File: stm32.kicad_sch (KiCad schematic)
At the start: 92 parts, among them J1 USB_B_Mini, J4 Conn_ST_STDC14, J5 Conn_02x20_Odd_Even, J7 TC2030 - TAG Connect, Q5 SI2301CDS-T1-GE3, SW1 SW_Push, SW2 SW_Push, U3 STM32F427V_G-I_Tx, X1 8MHz 20pF

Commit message: pre quilter - actually saved
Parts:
- U3: symbol MCU_ST_STM32F4:STM32F427V_G-I_Tx -> dnt:STM32F427V_G-I_Tx-mod
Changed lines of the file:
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@@
 			)
 		)
-		(property "Description" "20V 3.1A 112mΩ@4.5V,2.8A 1V@250uA 1PCSPChannel SOT-23 MOSFETs ROHS"
+		(property "Description" "Generic N-Channel Power MOSFET"
 			(at 349.25 193.04 0)
 			(effects
@@
 	)
 	(symbol
-		(lib_id "MCU_ST_STM32F4:STM32F427V_G-I_Tx")
+		(lib_id "dnt:STM32F427V_G-I_Tx-mod")
 		(at 163.83 158.75 0)
 		(unit 1)

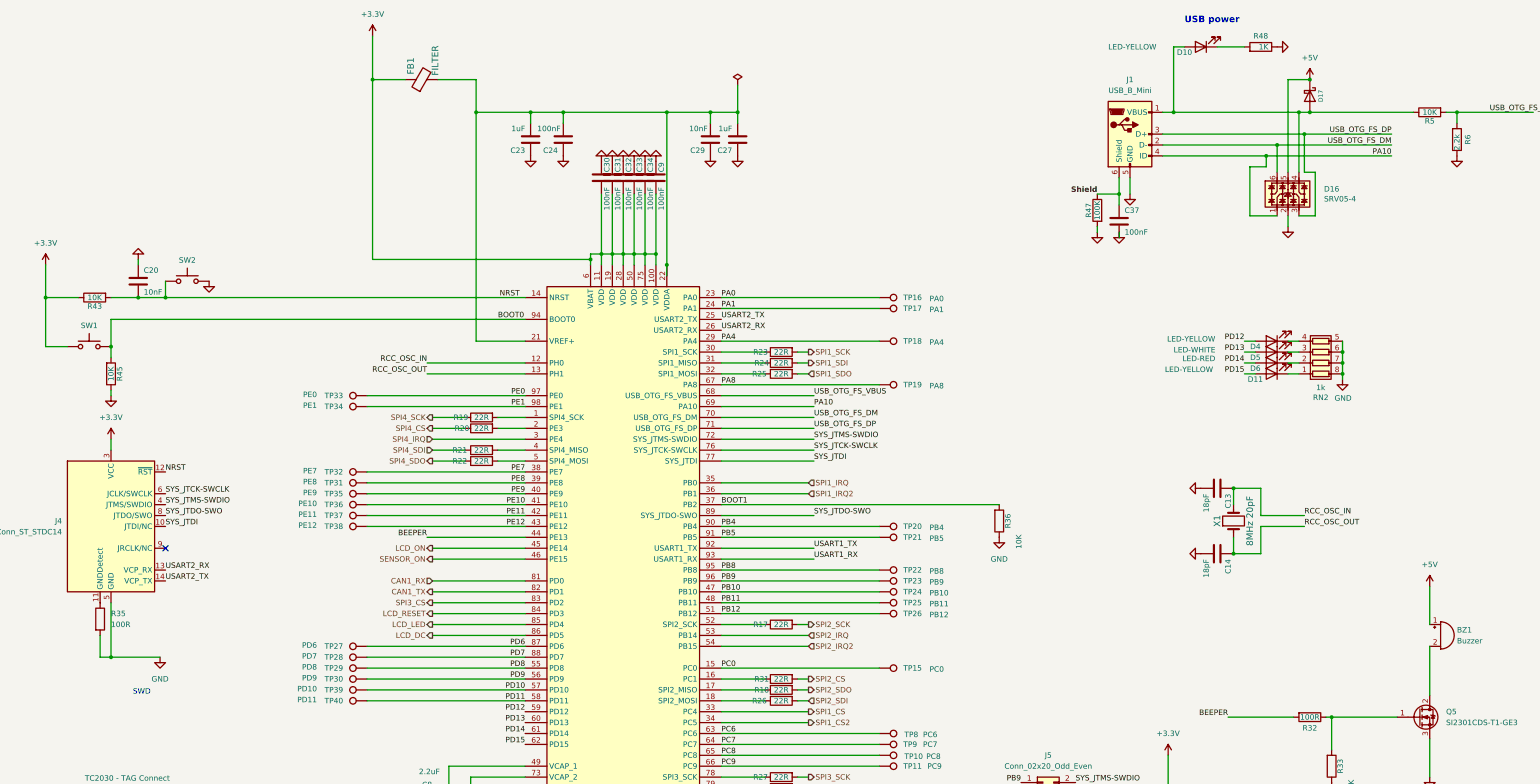
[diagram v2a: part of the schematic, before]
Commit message: smaller caps remove ringing resistors
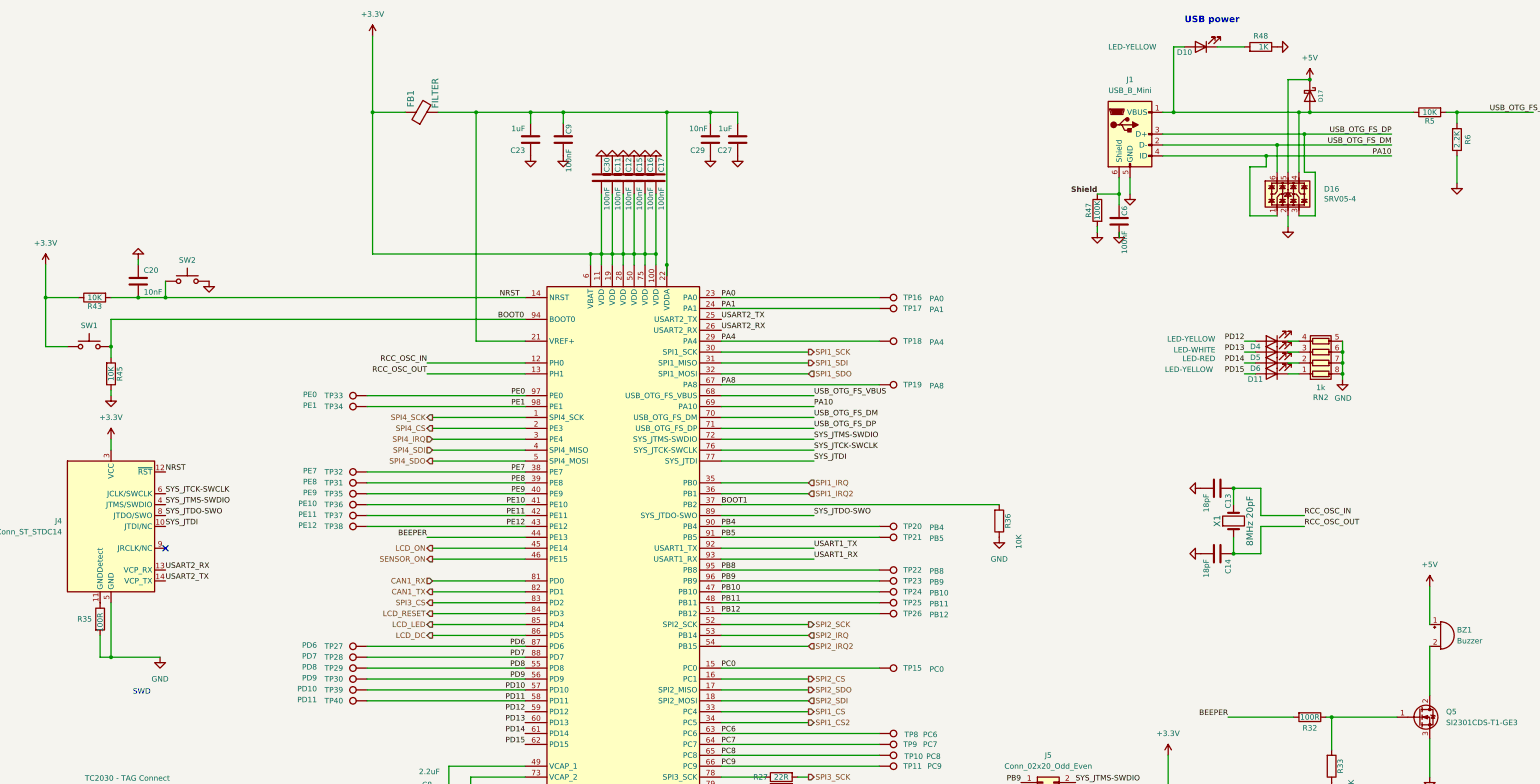
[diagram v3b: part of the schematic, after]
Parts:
- removed C24, C31, C32, C33, C34, C37: 100nF, Capacitor_SMD:C_0603_1608Metric, symbol Device:C
- removed R17, R18, R19, R20, R21, R22, R23, R24, R25, R26, R31: 22R, Resistor_SMD:R_0603_1608Metric, symbol Device:R
- added C11, C12, C15, C16, C17, C6: 100nF, Capacitor_SMD:C_01005_0402Metric, symbol Device:C
- C1: Manufacturer MURATA -> (none); PageName stm32f407_board -> (none); Part # GRM188R6YA225KA12D -> (none); VEND DIGI -> (none); VEND# 490-7204-1-ND -> (none)
- C13: PageName stm32f407_board -> (none); VEND DIGI -> (none); VEND# 1276-1089-1-ND -> (none)
- C14: PageName stm32f407_board -> (none); VEND DIGI -> (none); VEND# 1276-1089-1-ND -> (none); Voltage (none) -> 50V
- C20, C29: Manufacturer KEMET -> (none); Part # C0603C103K1RACTU -> (none); VEND DIGI -> (none); VEND# 399-3189-1-ND -> (none); Voltage (none) -> 50V
- C30, C9: footprint Capacitor_SMD:C_0603_1608Metric -> Capacitor_SMD:C_01005_0402Metric; LCSC C14663 -> C1525; Manufacturer KEMET -> Samsung; PageName stm32f407_board -> (none); Part # C0603C104J5RACTU -> (none); VEND DIGI -> (none); VEND# 399-7844-1-ND -> (none); Voltage (none) -> 16V
- R32: LCSC C21190 -> C22775; Manufacturer StackPole -> (none); Part # RMCF0603JJ1K00 -> (none); VEND DIGI -> (none); VEND# RMCF0603JJ1K00CT-ND -> (none)
- R33, R36, R43, R45, R5: Manufacturer StackPole -> (none); Part # RMCF0603JT10K0 -> (none); VEND DIGI -> (none); VEND# RMCF0603JT10K0CT-ND -> (none)
- R35: LCSC (none) -> C22775
- R47: Manufacturer StackPole -> (none); PageName stm32f407_board -> (none); Part # RMCF0603JT100K -> (none); VEND DIGI -> (none); VEND# RMCF0603JT100KCT-ND -> (none)
- R48: LCSC C4190 -> C21190
- R6: value 2.2k -> 2.2K; Manufacturer StackPole -> (none); PageName stm32f407_board -> (none); Part # RMCF0603FT2K20 -> (none); VEND DIGI -> (none); VEND# RMCF0603FT2K20CT-ND -> (none)
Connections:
- net +3.3V: now also C11.2, C12.2, C15.2, C16.2, C17.2; no longer C9.2
- net GND: now also C9.2, C11.1, C12.1, C15.1, C16.1, C17.1, C6.2; no longer C9.1
- net SPI1_SCK: now also U3.30 (PA5)
- net SPI1_SDI: now also U3.31 (PA6)
- net SPI1_SDO: now also U3.32 (PA7)
- net SPI2_CS: now also U3.16 (PC1)
- net SPI2_SCK: now also U3.52 (PB13)
- net SPI2_SDI: now also U3.18 (PC3)
- net SPI2_SDO: now also U3.17 (PC2)
- net SPI4_CS: now also U3.2 (PE3)
- net SPI4_SCK: now also U3.1 (PE2)
- net SPI4_SDI: now also U3.4 (PE5)
- net SPI4_SDO: now also U3.5 (PE6)
- net Shield: now also C6.1
- net at C23.2, C27.2, C29.2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: now also C9.1
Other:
- moved on the sheet: FB1

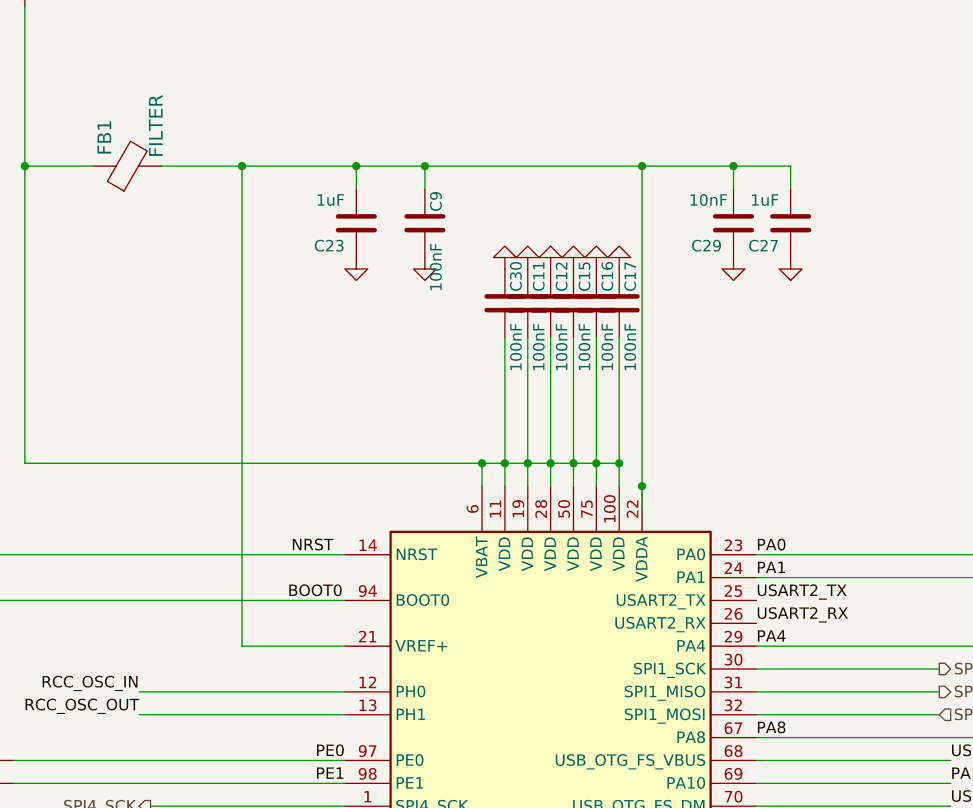
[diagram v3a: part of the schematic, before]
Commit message: add tp  move leds +
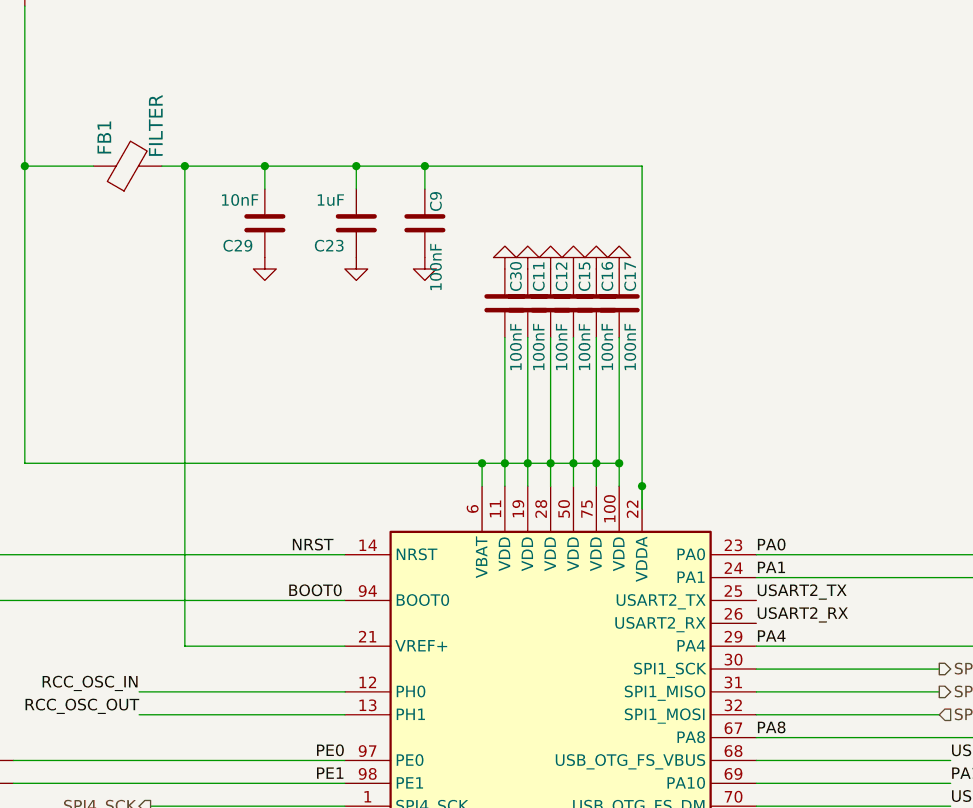
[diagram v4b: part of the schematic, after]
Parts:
- removed C27: 1uF, Capacitor_SMD:C_0603_1608Metric, symbol Device:C
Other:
- moved on the sheet: C29

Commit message: usb sheet
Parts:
- removed C6: 100nF, Capacitor_SMD:C_01005_0402Metric, symbol Device:C
- removed D10: LED-YELLOW, LED_SMD:LED_0603_1608Metric, symbol Device:LED
- removed D16: SRV05-4, Package_TO_SOT_SMD:SOT-363_SC-70-6, symbol Power_Protection:NUP4202
- removed D17: B5819W, Diode_SMD:D_SOD-123, symbol Device:D_Schottky
- removed J1: USB_B_Mini, dnt:USB-MINI-B-VERTICAL, symbol Connector:USB_B_Mini
- removed R47: 100K, Resistor_SMD:R_0603_1608Metric, symbol Device:R
- removed R48: 1K, Resistor_SMD:R_0603_1608Metric, symbol Device:R
- removed R5: 10K, Resistor_SMD:R_0603_1608Metric, symbol Device:R
- removed R6: 2.2K, Resistor_SMD:R_0603_1608Metric, symbol Device:R
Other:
- note removed: "USB power"

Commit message: smaller test pads
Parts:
- BZ1: LCSC c -> C96493
- TP10, TP11, TP12, TP13, TP14, TP15, TP16, TP17, TP18, TP19, TP20, TP21, TP22, TP23, TP24, TP25, TP26, TP27, TP28, TP29, TP30, TP31, TP32, TP33, TP34, TP35, TP36, TP37, TP38, TP39, TP40, TP8, TP9: footprint TestPoint:TestPoint_Pad_D1.0mm -> dnt:TestPoint_Pad_D1.0mm FP .6R

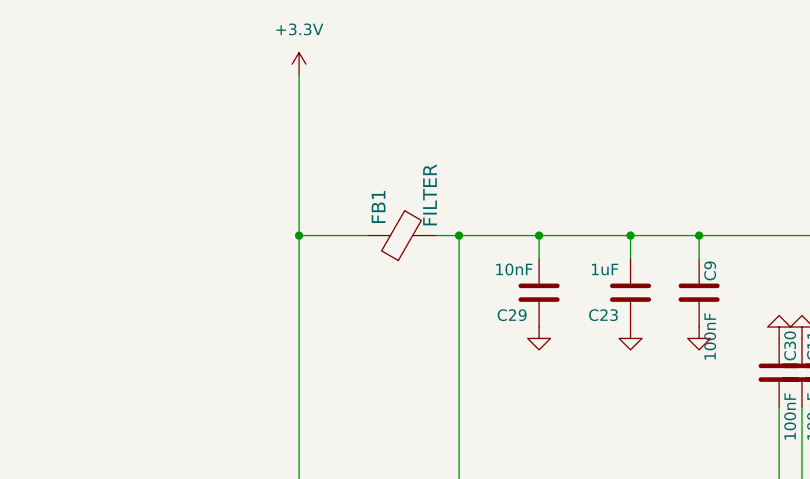
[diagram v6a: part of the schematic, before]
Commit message: pre-quilter after cap size issue
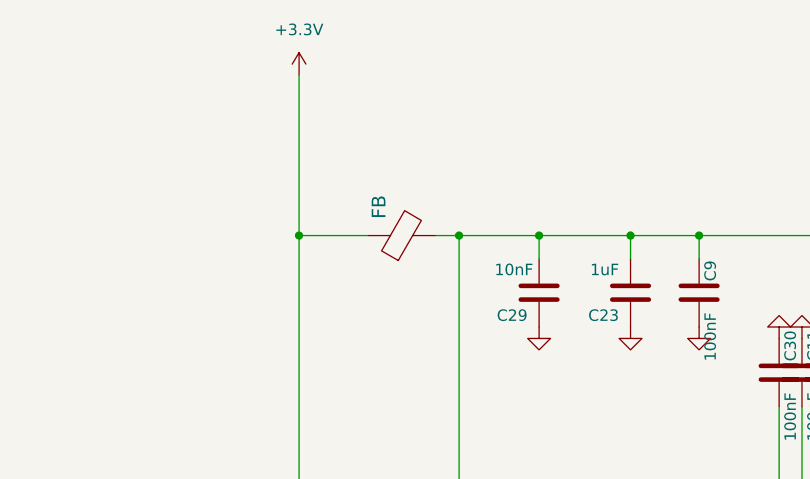
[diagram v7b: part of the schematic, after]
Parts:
- C11, C15, C16, C17, C30, C9: footprint Capacitor_SMD:C_01005_0402Metric -> Capacitor_SMD:C_0603_1608Metric; LCSC C1525 -> (none); Manufacturer Samsung -> (none); Voltage 16V -> (none)
- C12: footprint Capacitor_SMD:C_01005_0402Metric -> Capacitor_SMD:C_0603_1608Metric
- FB: renamed from FB1; value FILTER -> (none); footprint Resistor_SMD:R_0201_0603Metric -> Inductor_SMD:L_0603_1608Metric
- TP10, TP11, TP12, TP13, TP14, TP15, TP16, TP17, TP18, TP19, TP20, TP21, TP22, TP23, TP24, TP25, TP26, TP27, TP28, TP29, TP30, TP31, TP32, TP33, TP34, TP35, TP36, TP37, TP38, TP39, TP40, TP8, TP9: now left out of the parts list
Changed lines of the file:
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@@
 		(on_board yes)
 		(dnp no)
-		(property "Reference" "FB1"
+		(property "Reference" "FB"
 			(at 114.3 48.895 0)
 			(effects
@@
 			)
 		)
-		(property "Value" "FILTER"
+		(property "Value" ""
 			(at 120.015 47.625 0)
 			(effects
@@
 			)
 		)
-		(property "Footprint" "Resistor_SMD:R_0201_0603Metric"
+		(property "Footprint" "Inductor_SMD:L_0603_1608Metric"
 			(at 116.84 52.07 0)
 			(effects
@@
 			)
 		)
-		(property "Datasheet" ""
+		(property "Datasheet" "https://wmsc.lcsc.com/wmsc/upload/file/pdf/v2/lcsc/2310301641_Sunlord-SDFL1608Q4R7KTF_C1034.pdf"
 			(at 116.84 52.07 0)
 			(effects
@@
 					(size 1.524 1.524)
 				)
+				(hide yes)
 			)
 		)
@@
 			(project "l8-kicad"
 				(path "/8d063f79-9282-4820-bcf4-1ff3c006cf08/00000000-0000-0000-0000-00005d0250fb"
-					(reference "FB1")
+					(reference "FB")
 					(unit 1)
 				)
@@
 			)
 		)
-		(property "Footprint" "Capacitor_SMD:C_01005_0402Metric"
+		(property "Footprint" "Capacitor_SMD:C_0603_1608Metric"
 			(at 38.862 26.67 90)
 			(effects
@@
 			)
 		)
-		(property "LCSC" "C1525"
+		(property "LCSC" ""
 			(at 158.75 67.31 0)
 			(effects
@@
 			)
 		)
-		(property "Manufacturer" "Samsung"
+		(property "Manufacturer" ""
 			(at 158.75 67.31 0)
 			(effects
@@
 			)
 		)
-		(property "Voltage" "16V"
+		(property "Voltage" ""
 			(at 158.75 67.31 90)
 			(effects
@@
 		(unit 1)
 		(exclude_from_sim no)
-		(in_bom yes)
+		(in_bom no)
 		(on_board yes)
 		(dnp no)
@@
 		(unit 1)
 		(exclude_from_sim no)
-		(in_bom yes)
+		(in_bom no)
 		(on_board yes)
 		(dnp no)
@@
 			)
 		)
-		(property "Footprint" "Capacitor_SMD:C_01005_0402Metric"
+		(property "Footprint" "Capacitor_SMD:C_0603_1608Metric"
 			(at 41.402 26.67 90)
 			(effects
@@
 			)
 		)
-		(property "LCSC" "C1525"
+		(property "LCSC" ""
 			(at 161.29 67.31 0)
 			(effects
@@
 			)
 		)
-		(property "Manufacturer" "Samsung"
+		(property "Manufacturer" ""
 			(at 161.29 67.31 0)
 			(effects
@@
 			)
 		)
-		(property "Voltage" "16V"
+		(property "Voltage" ""
 			(at 161.29 67.31 90)
 			(effects
@@
 		(unit 1)
 		(exclude_from_sim no)
-		(in_bom yes)
+		(in_bom no)
 		(on_board yes)
 		(dnp no)
@@
 		(unit 1)
 		(exclude_from_sim no)
-		(in_bom yes)
+		(in_bom no)
 		(on_board yes)
 		(dnp no)
@@
 		(unit 1)
 		(exclude_from_sim no)
-		(in_bom yes)
+		(in_bom no)
 		(on_board yes)
 		(dnp no)
@@
 		(unit 1)
 		(exclude_from_sim no)
-		(in_bom yes)
+		(in_bom no)
 		(on_board yes)
 		(dnp no)
@@
 		(unit 1)
 		(exclude_from_sim no)
-		(in_bom yes)
+		(in_bom no)
 		(on_board yes)
 		(dnp no)
@@
 		(unit 1)
 		(exclude_from_sim no)
-		(in_bom yes)
+		(in_bom no)
 		(on_board yes)
 		(dnp no)
@@
 		(unit 1)
 		(exclude_from_sim no)
-		(in_bom yes)
+		(in_bom no)
 		(on_board yes)
 		(dnp no)
@@
 		(unit 1)
 		(exclude_from_sim no)
-		(in_bom yes)
+		(in_bom no)
 		(on_board yes)
 		(dnp no)
@@
 		(unit 1)
 		(exclude_from_sim no)
-		(in_bom yes)
+		(in_bom no)
 		(on_board yes)
 		(dnp no)
@@
 		(unit 1)
 		(exclude_from_sim no)
-		(in_bom yes)
+		(in_bom no)
 		(on_board yes)
 		(dnp no)
@@
 		(unit 1)
 		(exclude_from_sim no)
-		(in_bom yes)
+		(in_bom no)
 		(on_board yes)
 		(dnp no)
@@
 			)
 		)
-		(property "Footprint" "Capacitor_SMD:C_01005_0402Metric"
+		(property "Footprint" "Capacitor_SMD:C_0603_1608Metric"
 			(at 49.022 26.67 90)
 			(effects
@@
 			)
 		)
-		(property "LCSC" "C1525"
+		(property "LCSC" ""
 			(at 168.91 67.31 0)
 			(effects
@@
 			)
 		)
-		(property "Manufacturer" "Samsung"
+		(property "Manufacturer" ""
 			(at 168.91 67.31 0)
 			(effects
@@
 			)
 		)
-		(property "Voltage" "16V"
+		(property "Voltage" ""
 			(at 168.91 67.31 90)
 			(effects
@@
 		(unit 1)
 		(exclude_from_sim no)
-		(in_bom yes)
+		(in_bom no)
 		(on_board yes)
 		(dnp no)
@@
 		(unit 1)
 		(exclude_from_sim no)
-		(in_bom yes)
+		(in_bom no)
 		(on_board yes)
 		(dnp no)
@@
 		(unit 1)
 		(exclude_from_sim no)
-		(in_bom yes)
+		(in_bom no)
 		(on_board yes)
 		(dnp no)
@@
 		(unit 1)
 		(exclude_from_sim no)
-		(in_bom yes)
+		(in_bom no)
 		(on_board yes)
 		(dnp no)
@@
 		(unit 1)
 		(exclude_from_sim no)
-		(in_bom yes)
+		(in_bom no)
 		(on_board yes)
 		(dnp no)
@@
 		(unit 1)
 		(exclude_from_sim no)
-		(in_bom yes)
+		(in_bom no)
 		(on_board yes)
 		(dnp no)
@@
 			)
 		)
-		(property "Footprint" "Capacitor_SMD:C_01005_0402Metric"
+		(property "Footprint" "Capacitor_SMD:C_0603_1608Metric"
 			(at 43.942 26.67 90)
 			(effects
@@
 		(unit 1)
 		(exclude_from_sim no)
-		(in_bom yes)
+		(in_bom no)
 		(on_board no)
 		(dnp no)
@@
 		(unit 1)
 		(exclude_from_sim no)
-		(in_bom yes)
+		(in_bom no)
 		(on_board yes)
 		(dnp no)
@@
 		(unit 1)
 		(exclude_from_sim no)
-		(in_bom yes)
+		(in_bom no)
 		(on_board yes)
 		(dnp no)
@@
 		(unit 1)
 		(exclude_from_sim no)
-		(in_bom yes)
+		(in_bom no)
 		(on_board yes)
 		(dnp no)
@@
 		(unit 1)
 		(exclude_from_sim no)
-		(in_bom yes)
+		(in_bom no)
 		(on_board yes)
 		(dnp no)
@@
 			)
 		)
-		(property "Footprint" "Capacitor_SMD:C_01005_0402Metric"
+		(property "Footprint" "Capacitor_SMD:C_0603_1608Metric"
 			(at 51.562 26.67 90)
 			(effects
@@
 			)
 		)
-		(property "LCSC" "C1525"
+		(property "LCSC" ""
 			(at 171.45 67.31 0)
 			(effects
@@
 			)
 		)
-		(property "Manufacturer" "Samsung"
+		(property "Manufacturer" ""
 			(at 171.45 67.31 0)
 			(effects
@@
 			)
 		)
-		(property "Voltage" "16V"
+		(property "Voltage" ""
 			(at 171.45 67.31 90)
 			(effects
@@
 		(unit 1)
 		(exclude_from_sim no)
-		(in_bom yes)
+		(in_bom no)
 		(on_board yes)
 		(dnp no)
@@
 			)
 		)
-		(property "Footprint" "Capacitor_SMD:C_01005_0402Metric"
+		(property "Footprint" "Capacitor_SMD:C_0603_1608Metric"
 			(at 29.972 17.78 90)
 			(effects
@@
 			)
 		)
-		(property "LCSC" "C1525"
+		(property "LCSC" ""
 			(at 149.86 58.42 0)
 			(effects
@@
 			)
 		)
-		(property "Manufacturer" "Samsung"
+		(property "Manufacturer" ""
 			(at 149.86 58.42 0)
 			(effects
@@
 			)
 		)
-		(property "Voltage" "16V"
+		(property "Voltage" ""
 			(at 149.86 58.42 90)
 			(effects
@@
 		(unit 1)
 		(exclude_from_sim no)
-		(in_bom yes)
+		(in_bom no)
 		(on_board yes)
 		(dnp no)
@@
 		(unit 1)
 		(exclude_from_sim no)
-		(in_bom yes)
+		(in_bom no)
 		(on_board yes)
 		(dnp no)
@@
 			)
 		)
-		(property "Footprint" "Capacitor_SMD:C_01005_0402Metric"
+		(property "Footprint" "Capacitor_SMD:C_0603_1608Metric"
 			(at 46.482 26.67 90)
 			(effects
@@
 			)
 		)
-		(property "Description" "Unpolarized capacitor X7R"
+		(property "Description" "Unpolarized capacitor X7R 603"
 			(at 166.37 67.31 0)
 			(effects
@@
 			)
 		)
-		(property "LCSC" "C1525"
+		(property "LCSC" ""
 			(at 166.37 67.31 0)
 			(effects
@@
 			)
 		)
-		(property "Manufacturer" "Samsung"
+		(property "Manufacturer" ""
 			(at 166.37 67.31 0)
 			(effects
@@
 			)
 		)
-		(property "Voltage" "16V"
+		(property "Voltage" ""
 			(at 166.37 67.31 90)
 			(effects
@@
 		(unit 1)
 		(exclude_from_sim no)
-		(in_bom yes)
+		(in_bom no)
 		(on_board yes)
 		(dnp no)
@@
 		(unit 1)
 		(exclude_from_sim no)
-		(in_bom yes)
+		(in_bom no)
 		(on_board yes)
 		(dnp no)
@@
 		(unit 1)
 		(exclude_from_sim no)
-		(in_bom yes)
+		(in_bom no)
 		(on_board yes)
 		(dnp no)
@@
 		(unit 1)
 		(exclude_from_sim no)
-		(in_bom yes)
+		(in_bom no)
 		(on_board yes)
 		(dnp no)
@@
 		(unit 1)
 		(exclude_from_sim no)
-		(in_bom yes)
+		(in_bom no)
 		(on_board yes)
 		(dnp no)
@@
 		(unit 1)
 		(exclude_from_sim no)
-		(in_bom yes)
+		(in_bom no)
 		(on_board yes)
 		(dnp no)
